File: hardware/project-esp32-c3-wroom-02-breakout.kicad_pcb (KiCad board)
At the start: 4 copper layers, 25.4 x 24.4 mm, 19 parts, among them J1 SM04B-SRSS-TB(LF)(SN), J2 Conn_01x08_Male, J3 Conn_01x08_Male, Q1 MUN5214DW1T1G, U1 XC6220B331MR, U2 ESP32-C3-WROOM-02-H4

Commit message: First placement done
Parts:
- removed C6: 22pF, Capacitor_SMD:C_0603_1608Metric_Pad1.08x0.95mm_HandSolder
- removed JP1: SolderJumper_3_Bridged12, Jumper:SolderJumper-3_P1.3mm_Bridged12_RoundedPad1.0x1.5mm
- added C3: 0.1uF, Capacitor_SMD:C_0603_1608Metric_Pad1.08x0.95mm_HandSolder, F.Cu at (46.7, 49.0)
- added D2: CUS10S30,H3F‎, Diode_SMD:D_SOD-323, F.Cu at (49.5, 57.4)
- added H1: MountingHole_Pad, MountingHole:MountingHole_2.2mm_M2_ISO7380_Pad, F.Cu at (39.9, 65.5)
- added H2: MountingHole_Pad, MountingHole:MountingHole_2.2mm_M2_ISO7380_Pad, F.Cu at (60.2, 65.5)
- added J4: USB4105-GF-A, USB4105-GF-A:GCT_USB4105-GF-A, F.Cu at (52.6, 66.0)
- added Q2: Q_PMOS_DGS, SSM6J214FE-TE85L-F:SOT50P160X60-6N, F.Cu at (42.2, 52.8)
- added R7: 100k, Resistor_SMD:R_0603_1608Metric_Pad0.98x0.95mm_HandSolder, F.Cu at (54.4, 55.1)
- added R8: 5.1k, Resistor_SMD:R_0603_1608Metric_Pad0.98x0.95mm_HandSolder, F.Cu at (60.2, 62.5)
- added R9: 5.1k, Resistor_SMD:R_0603_1608Metric_Pad0.98x0.95mm_HandSolder, F.Cu at (60.2, 61.0)
- added TP1: TestPoint, TestPoint:TestPoint_Pad_D1.0mm, F.Cu at (52.1, 58.4)
- added TP2: TestPoint, TestPoint:TestPoint_Pad_D1.0mm, F.Cu at (53.6, 58.4)
- added TP3: TestPoint, TestPoint:TestPoint_Pad_D1.0mm, F.Cu at (57.4, 58.4)
- C1, C4: value 10uF -> 22uF
- C5: value 22pF -> 22uF; footprint Capacitor_SMD:C_0603_1608Metric_Pad1.08x0.95mm_HandSolder -> Capacitor_SMD:C_0805_2012Metric_Pad1.18x1.45mm_HandSolder
- J3: value Conn_01x08_Male -> Conn_01x10_Male; footprint Connector_PinHeader_2.54mm:PinHeader_1x08_P2.54mm_Vertical -> Connector_PinHeader_2.54mm:PinHeader_1x10_P2.54mm_Vertical
- R4, R5: value 4k7 -> 5.1k
- R6: value 10k -> 5.1k
- moved D1 19.8 mm to (43.9, 65.0)
- moved R2 16.9 mm to (58.4, 50.3)
- moved R3 16.9 mm to (56.9, 50.3)
- moved R6 16.6 mm to (45.7, 65.0)
- moved R4 15.2 mm to (45.7, 58.9)
- moved J1 13.9 mm to (42.4, 59.2), turned to 270 degrees
- moved R1 12.6 mm to (55.4, 50.3)
- moved R5 11.5 mm to (45.7, 57.4), turned to 180 degrees
- moved C5 11.0 mm to (42.9, 49.3)
- moved C2 9.72 mm to (53.6, 50.3)
- moved Q1 8.92 mm to (57.9, 54.9)
- moved C1 3.61 mm to (44.7, 53.1)
- moved C4 3.61 mm to (50.3, 53.1)
- moved U1 3.61 mm to (47.5, 53.1)
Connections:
- C1 pad 1: VCC -> Net-(C1-Pad1)
- C5 pad 1: /USB_D+ -> +3V3
- J1 pad 2: Net-(J1-Pad2) -> +3V3
- J1 pad 3: /USB_D+ -> /SDA
- J1 pad 4: /USB_D- -> /SCL
- J2 pad 5: /GPIO6 -> /SDA
- J2 pad 6: /GPIO7 -> /SCL
- J2 pad 7: VCC -> +BATT
- R4 pad 2: /USB_D- -> /SCL
- R5 pad 2: /USB_D+ -> /SDA
- U1 pad 1: VCC -> Net-(C1-Pad1)
- U1 pad 3: VCC -> Net-(C1-Pad1)
- U2 pad 5: /GPIO6 -> /SDA
- U2 pad 6: /GPIO7 -> /SCL
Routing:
- net /GPIO2: track 30.3 -> 0.00 mm, vias 2 -> 0
- net /RESET: track 29.4 -> 3.46 mm, vias 2 -> 0
- net /DTR: track 19.7 -> 0.00 mm, vias 1 -> 0
- net /GPIO9: track 19.4 -> 0.00 mm, vias 2 -> 0
- net /RTS: track 19.0 -> 0.00 mm, vias 1 -> 0
- net /GPIO8: track 16.2 -> 0.00 mm, vias 2 -> 0
- net +3V3: track 17.3 -> 3.03 mm, vias 5 -> 0
- net /USB_D+: track 14.3 -> 23.8 mm
- net /USB_D-: track 12.8 -> 21.9 mm
- net Net-(J1-Pad2): track 9.11 -> 0.00 mm
- net GND: track 24.3 -> 15.3 mm, vias 11 -> 2
- net /GPIO7: track 8.84 -> 0.00 mm, vias 1 -> 0
- net /SDA: track 0.00 -> 6.33 mm
- net /GPIO6: track 6.33 -> 0.00 mm
- net Net-(D1-Pad2): track 1.79 -> 0.00 mm
- removed copper zone on F.Cu, net VCC
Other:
- board size 25.4 x 24.4 mm -> 25.4 x 34.3 mm

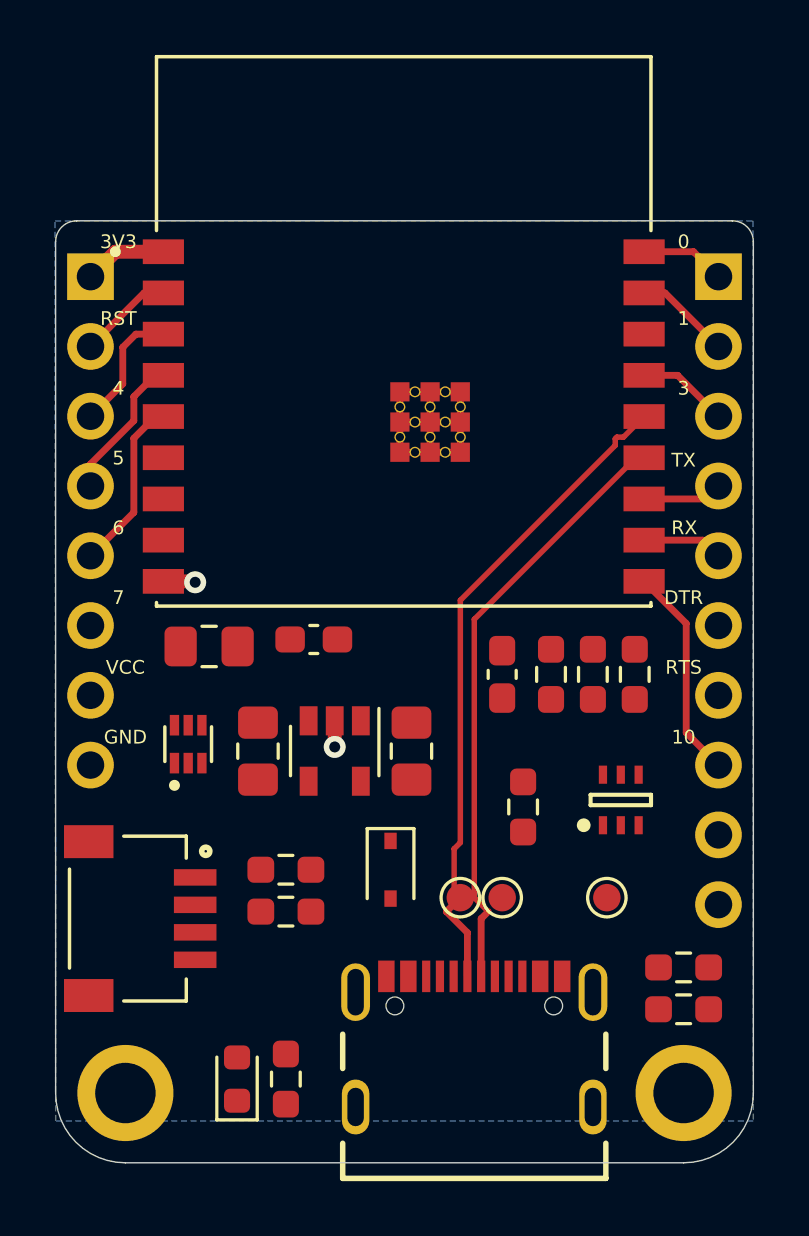
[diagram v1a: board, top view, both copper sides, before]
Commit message: Power + USB route
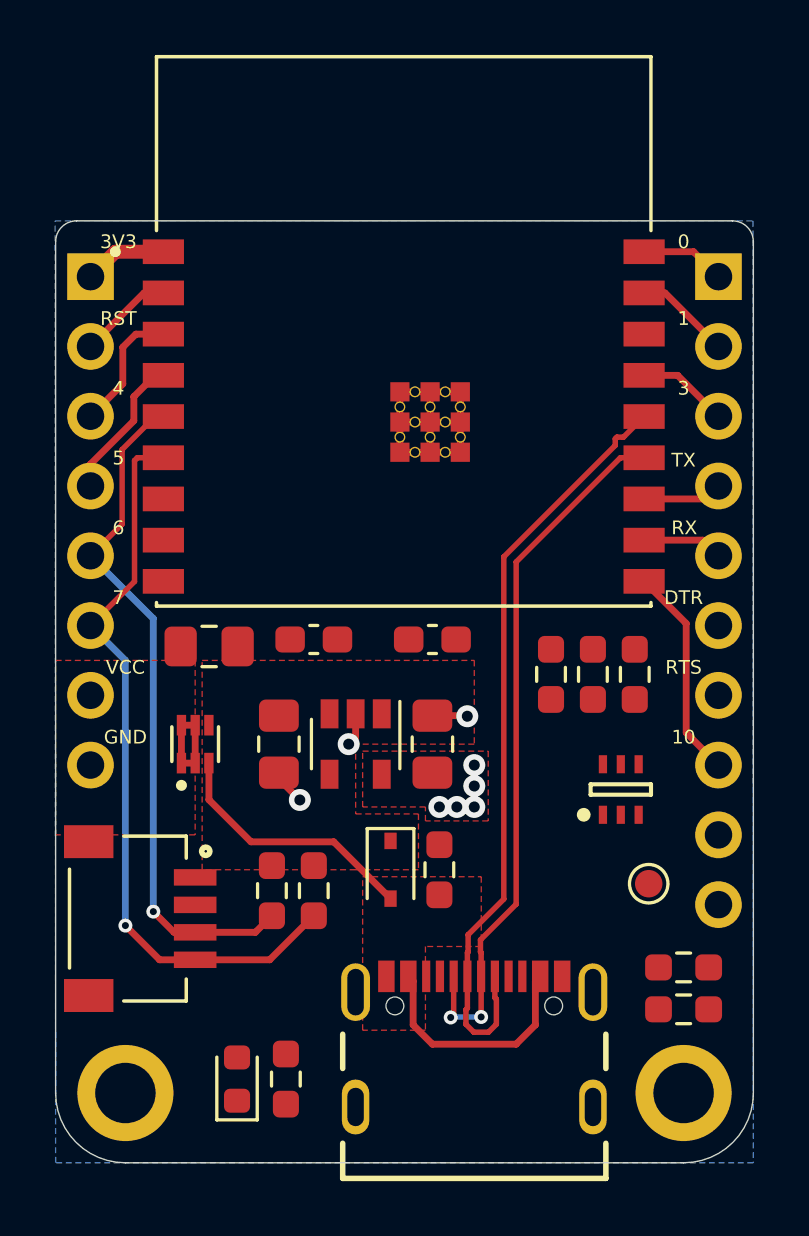
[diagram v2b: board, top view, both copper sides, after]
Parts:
- removed TP1, TP2: TestPoint, TestPoint:TestPoint_Pad_D1.0mm
- moved R7 3.81 mm to (51.3, 57.4)
- moved C2 2.84 mm to (51.1, 49.0), turned to 180 degrees
- moved TP3 1.61 mm to (58.9, 57.9)
- moved R4 1.27 mm to (46.7, 58.2), turned to 270 degrees
- moved R5 0.92 mm to (45.2, 58.2), turned to 270 degrees
- moved C1 0.80 mm to (45.5, 52.8)
- moved C4 0.80 mm to (51.1, 52.8)
- moved U1 0.80 mm to (48.3, 52.8)
- moved Q1 0.38 mm to (57.9, 54.5)
- moved Q2 0.25 mm to (42.4, 52.8)
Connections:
- net Net-(C1-Pad1) renamed /VIN
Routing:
- net /SCL: track 0.00 -> 27.2 mm, vias 0 -> 1
- net /SDA: track 6.33 -> 25.1 mm, vias 0 -> 1
- net VBUS: track 0.00 -> 18.1 mm
- net /USB_D+: track 23.8 -> 28.1 mm
- net /USB_D-: track 21.9 -> 26.0 mm, vias 0 -> 2
- net +BATT: track 0.00 -> 3.76 mm
- net GND: track 15.3 -> 17.0 mm, vias 2 -> 3
- net +3V3: vias 0 -> 5
- added copper zone on F.Cu, net +3V3
- added copper zone on F.Cu, net +BATT
- added copper zone on F.Cu, net /VIN
- added copper zone on F.Cu, net VBUS

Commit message: Routing done
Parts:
- moved TP3 0.57 mm to (58.4, 58.2)
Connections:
- J3 pad 6: /DTR -> /RTS
- J3 pad 7: /RTS -> /DTR
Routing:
- net /RESET: track 3.46 -> 30.3 mm, vias 0 -> 2
- net /GPIO9: track 0.00 -> 25.6 mm, vias 0 -> 2
- net GND: track 17.0 -> 36.1 mm, vias 3 -> 14
- net /GPIO8: track 0.00 -> 18.4 mm, vias 0 -> 2
- net /GPIO2: track 0.00 -> 13.7 mm, vias 0 -> 2
- net /CC1: track 0.00 -> 11.5 mm, vias 0 -> 2
- net +3V3: track 3.03 -> 13.7 mm, vias 5 -> 14
- net /RTS: track 0.00 -> 9.23 mm, vias 0 -> 1
- net /CC2: track 0.00 -> 6.62 mm
- net /DTR: track 0.00 -> 6.27 mm, vias 0 -> 1
- net Net-(D1-Pad2): track 0.00 -> 1.83 mm
- net /SDA: track 25.1 -> 26.1 mm
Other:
- board text added: "François Gervais 8 Jan. 2022 rev"
- board text removed: "François Gervais 25 sept. 2021 rev 1.0"

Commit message: Add version of previous commit
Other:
- board text added: "François Gervais 8 Jan. 2022 rev v2.0"
- board text removed: "François Gervais 8 Jan. 2022 rev"
